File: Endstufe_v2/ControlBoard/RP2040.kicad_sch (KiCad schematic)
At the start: 33 parts, among them J5 DNP, J7 DNP, SW1 TS-1187A-B-A-B, SW2 TS-1187A-B-A-B, U2 TYPE-C 16PFS 2JCB1.2-H6.5 IPX8, U3 W25Q128JVS, U4 RP2040, Y1 12Mhz

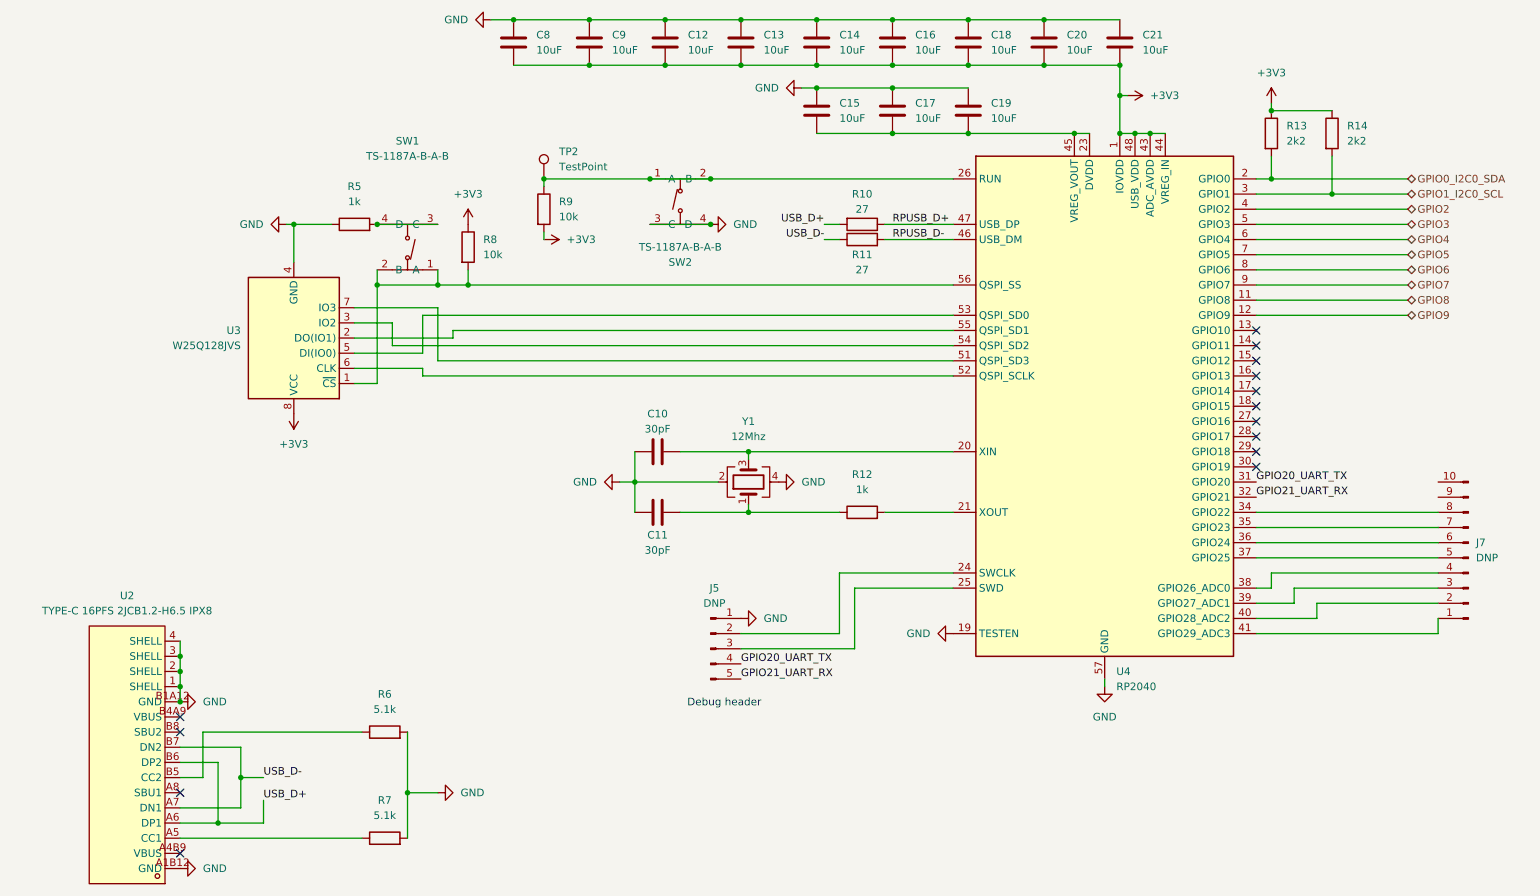
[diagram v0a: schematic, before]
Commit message: Added ADAU1962A DAC schematic
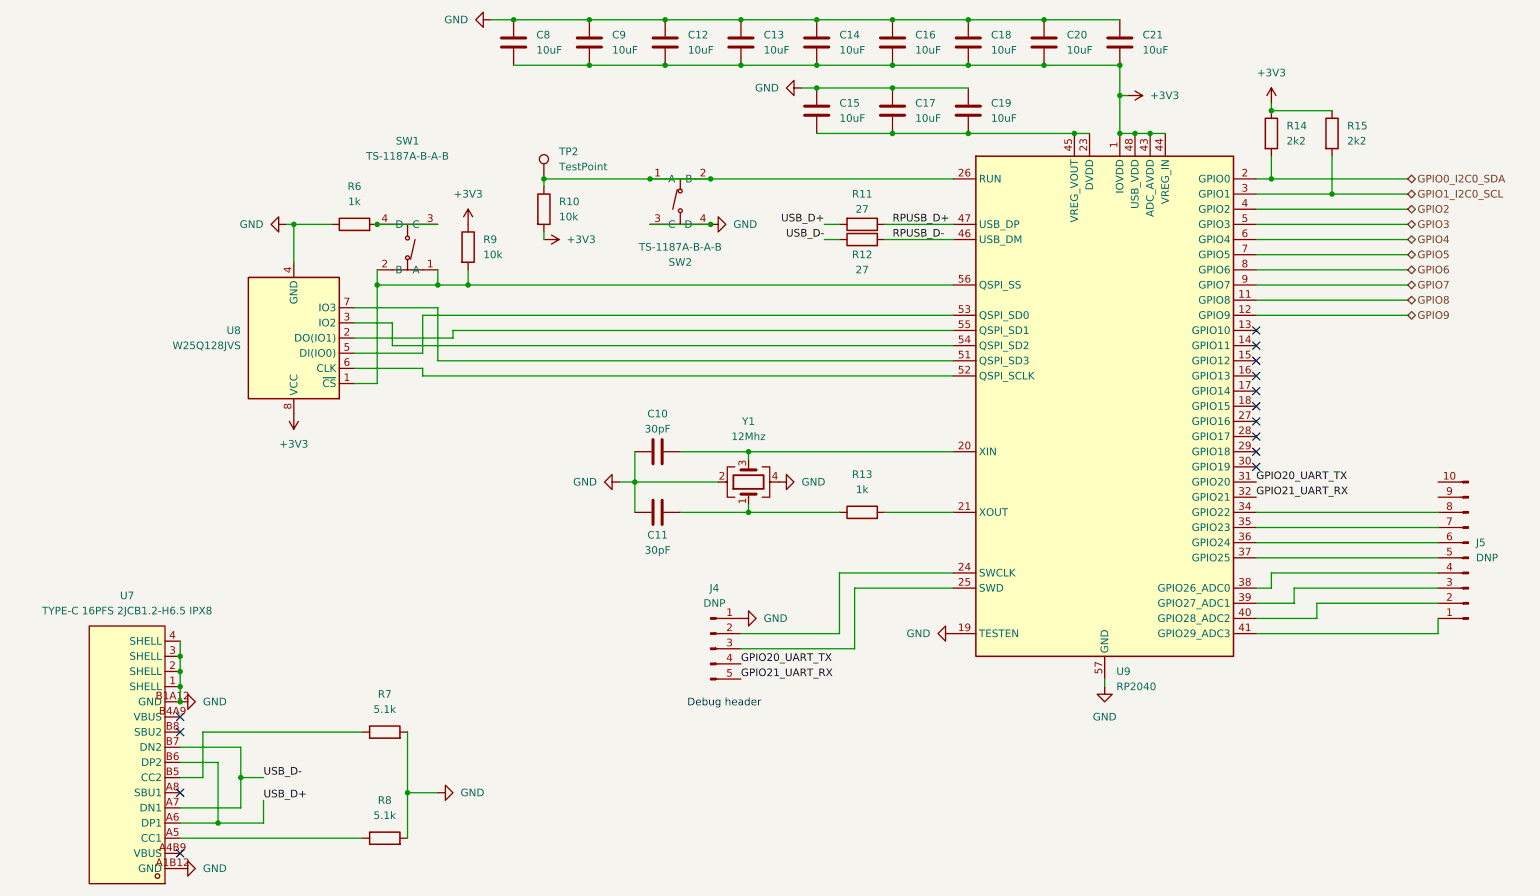
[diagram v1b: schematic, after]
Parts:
- renumbered J5 to J4, J7 to J5, R9 to R10, R10 to R11, R11 to R12, R12 to R13, R13 to R14, R14 to R15, R5 to R6, R6 to R7, R7 to R8, R8 to R9, U2 to U7, U3 to U8, U4 to U9

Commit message: Add footprints to all components
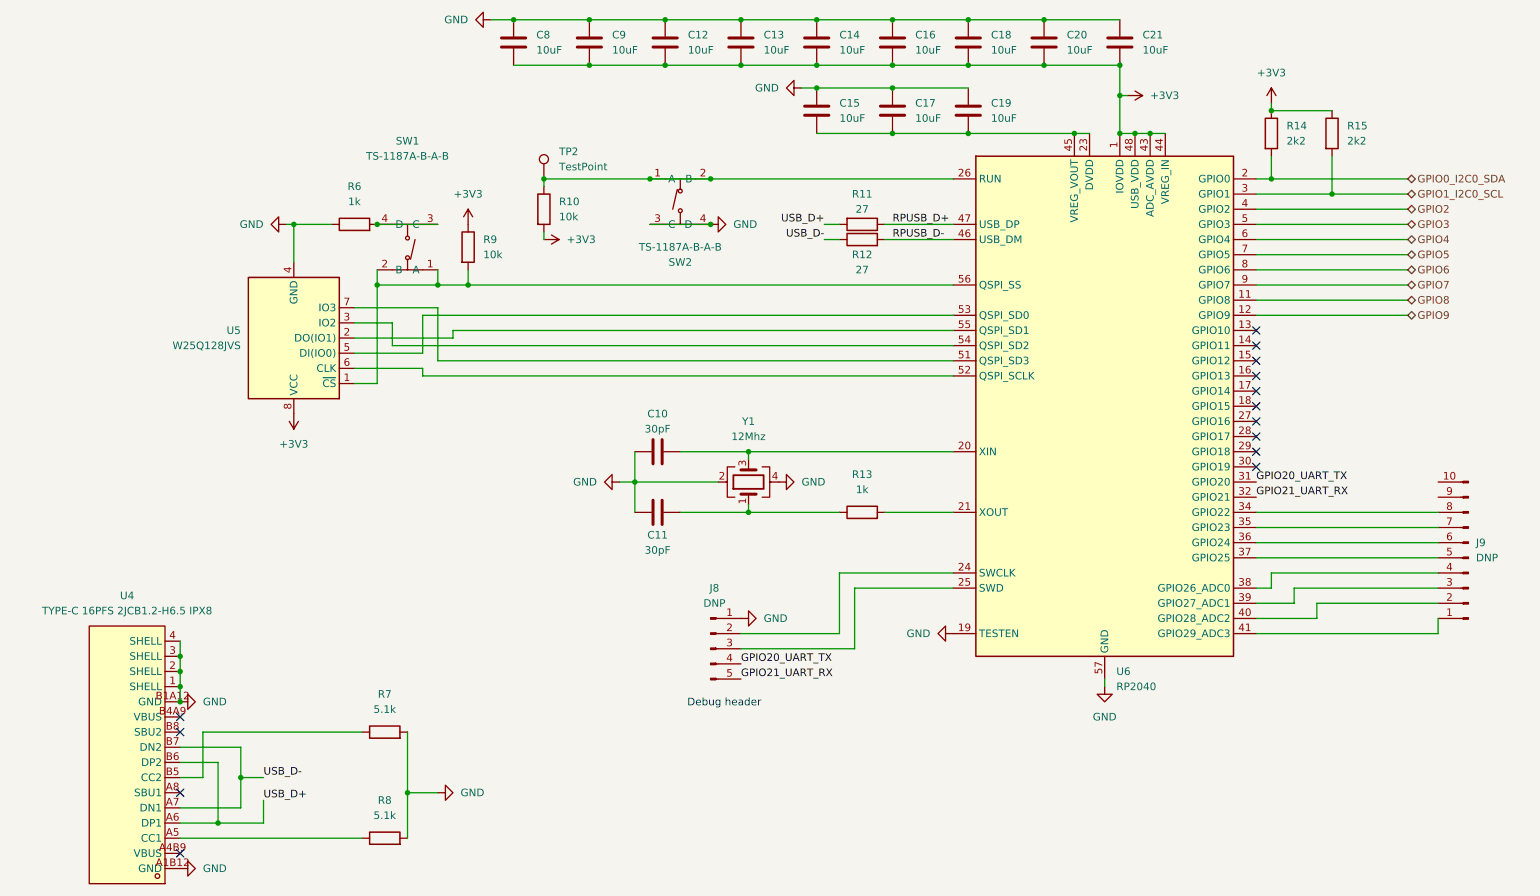
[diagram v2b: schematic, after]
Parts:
- J8: renamed from J4; footprint (none) -> Connector_PinHeader_2.54mm:PinHeader_1x05_P2.54mm_Vertical
- TP2: footprint (none) -> TestPoint:TestPoint_Pad_D1.0mm
- renumbered J5 to J9, U7 to U4, U8 to U5, U9 to U6
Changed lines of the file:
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@@
 		(dnp no)
 		(fields_autoplaced yes)
-		(property "Reference" "U7"
+		(property "Reference" "U4"
 			(at 36.83 123.19 0)
 			(effects
@@
 			(project "ControlBoard"
 				(path "/4f887f51-77c1-41d4-a3eb-45d362caffe1/2f61df4a-6dcc-4468-b102-34f7c082e72d"
-					(reference "U7")
+					(reference "U4")
 					(unit 1)
 				)
@@
 			)
 		)
-		(property "Footprint" ""
+		(property "Footprint" "TestPoint:TestPoint_Pad_D1.0mm"
 			(at 111.76 53.34 0)
 			(effects
@@
 		(dnp no)
 		(fields_autoplaced yes)
-		(property "Reference" "U9"
+		(property "Reference" "U6"
 			(at 202.6159 135.89 0)
 			(effects
@@
 			(project "ControlBoard"
 				(path "/4f887f51-77c1-41d4-a3eb-45d362caffe1/2f61df4a-6dcc-4468-b102-34f7c082e72d"
-					(reference "U9")
+					(reference "U6")
 					(unit 1)
 				)
@@
 		(on_board yes)
 		(dnp no)
-		(property "Reference" "J4"
+		(property "Reference" "J8"
 			(at 135.255 121.92 0)
 			(effects
@@
 			)
 		)
-		(property "Footprint" ""
+		(property "Footprint" "Connector_PinHeader_2.54mm:PinHeader_1x05_P2.54mm_Vertical"
 			(at 134.62 132.08 0)
 			(effects
@@
 			(project "ControlBoard"
 				(path "/4f887f51-77c1-41d4-a3eb-45d362caffe1/2f61df4a-6dcc-4468-b102-34f7c082e72d"
-					(reference "J4")
+					(reference "J8")
 					(unit 1)
 				)
@@
 		(dnp no)
 		(fields_autoplaced yes)
-		(property "Reference" "J5"
+		(property "Reference" "J9"
 			(at 262.89 114.3 0)
 			(effects
@@
 			(project "ControlBoard"
 				(path "/4f887f51-77c1-41d4-a3eb-45d362caffe1/2f61df4a-6dcc-4468-b102-34f7c082e72d"
-					(reference "J5")
+					(reference "J9")
 					(unit 1)
 				)
@@
 		(dnp no)
 		(fields_autoplaced yes)
-		(property "Reference" "U8"
+		(property "Reference" "U5"
 			(at 55.88 78.74 0)
 			(effects
@@
 			(project "ControlBoard"
 				(path "/4f887f51-77c1-41d4-a3eb-45d362caffe1/2f61df4a-6dcc-4468-b102-34f7c082e72d"
-					(reference "U8")
-					(unit 1)
-				)
+					(reference "U5")
+					(unit 1)
+				)

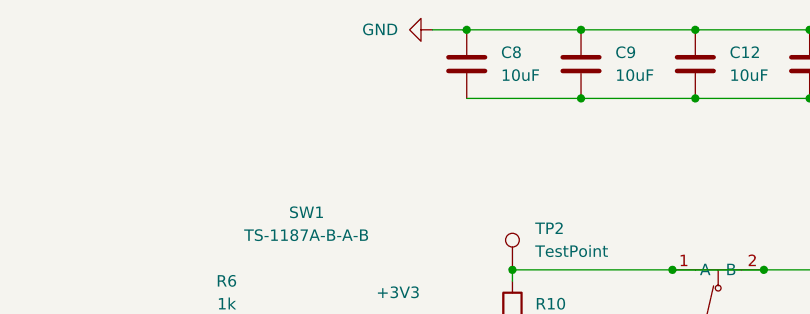
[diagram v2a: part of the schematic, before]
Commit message: Rough layout of components
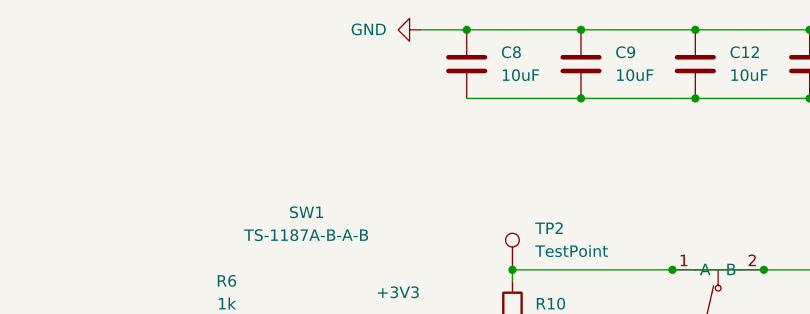
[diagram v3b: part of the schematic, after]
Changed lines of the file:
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@@
 	)
 	(junction
+		(at 114.3 34.29)
+		(diameter 0)
+		(color 0 0 0 0)
+	)
+	(junction
 		(at 152.4 38.1)
 		(diameter 0)
@@
 	)
 	(junction
-		(at 114.3 34.29)
-		(diameter 0)
-		(color 0 0 0 0)
-	)
-	(junction
 		(at 228.6 41.91)
 		(diameter 0)
@@
 	(wire
 		(pts
-			(xy 101.6 26.67) (xy 114.3 26.67)
+			(xy 96.52 26.67) (xy 101.6 26.67)
 		)
 		(stroke
@@
 	(wire
 		(pts
+			(xy 101.6 26.67) (xy 114.3 26.67)
+		)
+		(stroke
+			(width 0)
+			(type default)
+		)
+	)
+	(wire
+		(pts
 			(xy 83.82 156.21) (xy 88.9 156.21)
 		)
@@
 	(wire
 		(pts
+			(xy 101.6 34.29) (xy 114.3 34.29)
+		)
+		(stroke
+			(width 0)
+			(type default)
+		)
+	)
+	(wire
+		(pts
 			(xy 91.44 78.74) (xy 175.26 78.74)
 		)
@@
 	(wire
 		(pts
-			(xy 101.6 34.29) (xy 114.3 34.29)
-		)
-		(stroke
-			(width 0)
-			(type default)
-		)
-	)
-	(wire
-		(pts
 			(xy 78.74 68.58) (xy 78.74 71.12)
 		)
@@
 	(wire
 		(pts
-			(xy 97.79 26.67) (xy 101.6 26.67)
-		)
-		(stroke
-			(width 0)
-			(type default)
-		)
-	)
-	(wire
-		(pts
 			(xy 140.97 99.06) (xy 140.97 100.33)
 		)
@@
 	(symbol
 		(lib_id "Endstufe:C")
+		(at 101.6 30.48 0)
+		(unit 1)
+		(exclude_from_sim no)
+		(in_bom yes)
+		(on_board yes)
+		(dnp no)
+		(fields_autoplaced yes)
+		(property "Reference" "C8"
+			(at 105.41 29.21 0)
+			(effects
+				(font
+					(size 1.27 1.27)
+				)
+				(justify left)
+			)
+		)
+		(property "Value" "10uF"
+			(at 105.41 31.75 0)
+			(effects
+				(font
+					(size 1.27 1.27)
+				)
+				(justify left)
+			)
+		)
+		(property "Footprint" "Endstufe:C_0402_1005Metric"
+			(at 102.5652 34.29 0)
+			(effects
+				(font
+					(size 1.27 1.27)
+				)
+				(hide yes)
+			)
+		)
+		(property "Datasheet" "~"
+			(at 101.6 30.48 0)
+			(effects
+				(font
+					(size 1.27 1.27)
+				)
+				(hide yes)
+			)
+		)
+		(property "Description" ""
+			(at 101.6 30.48 0)
+			(effects
+				(font
+					(size 1.27 1.27)
+				)
+				(hide yes)
+			)
+		)
+		(property "LCSC Part #" "C15525"
+			(at 101.6 30.48 0)
+			(effects
+				(font
+					(size 1.27 1.27)
+				)
+				(hide yes)
+			)
+		)
+		(pin "1"
+		)
+		(pin "2"
+		)
+		(instances
+			(project "ControlBoard"
+				(path "/4f887f51-77c1-41d4-a3eb-45d362caffe1/2f61df4a-6dcc-4468-b102-34f7c082e72d"
+					(reference "C8")
+					(unit 1)
+				)
+			)
+		)
+	)
+	(symbol
+		(lib_id "Endstufe:C")
 		(at 165.1 41.91 0)
 		(unit 1)
@@
 	(symbol
 		(lib_id "Endstufe:GND")
-		(at 97.79 26.67 270)
+		(at 96.52 26.67 270)
 		(unit 1)
 		(exclude_from_sim no)
@@
 		(fields_autoplaced yes)
 		(property "Reference" "#PWR025"
-			(at 91.44 26.67 0)
+			(at 90.17 26.67 0)
 			(effects
 				(font
@@
 		)
 		(property "Value" "GND"
-			(at 93.98 26.67 90)
+			(at 92.71 26.67 90)
 			(effects
 				(font
@@
 		)
 		(property "Footprint" ""
-			(at 97.79 26.67 0)
+			(at 96.52 26.67 0)
 			(effects
 				(font
@@
 		)
 		(property "Datasheet" ""
-			(at 97.79 26.67 0)
+			(at 96.52 26.67 0)
 			(effects
 				(font
@@
 		)
 		(property "Description" ""
-			(at 97.79 26.67 0)
+			(at 96.52 26.67 0)
 			(effects
 				(font
@@
 					(unit 1)
 				)
-			)
-		)
-	)
-	(symbol
-		(lib_id "Endstufe:C")
-		(at 101.6 30.48 0)
-		(unit 1)
-		(exclude_from_sim no)
-		(in_bom yes)
-		(on_board yes)
-		(dnp no)
-		(fields_autoplaced yes)
-		(property "Reference" "C8"
-			(at 105.41 29.21 0)
-			(effects
-				(font
-					(size 1.27 1.27)
-				)
-				(justify left)
-			)
-		)
-		(property "Value" "10uF"
-			(at 105.41 31.75 0)
-			(effects
-				(font
-					(size 1.27 1.27)
-				)
-				(justify left)
-			)
-		)
-		(property "Footprint" "Endstufe:C_0402_1005Metric"
-			(at 102.5652 34.29 0)
-			(effects
-				(font
-					(size 1.27 1.27)
-				)
-				(hide yes)
-			)
-		)
-		(property "Datasheet" "~"
-			(at 101.6 30.48 0)
-			(effects
-				(font
-					(size 1.27 1.27)
-				)
-				(hide yes)
-			)
-		)
-		(property "Description" ""
-			(at 101.6 30.48 0)
-			(effects
-				(font
-					(size 1.27 1.27)
-				)
-				(hide yes)
-			)
-		)
-		(property "LCSC Part #" "C15525"
-			(at 101.6 30.48 0)
-			(effects
-				(font
-					(size 1.27 1.27)
-				)
-				(hide yes)
-			)
-		)
-		(pin "1"
-		)
-		(pin "2"
-		)
-		(instances
-			(project "ControlBoard"
-				(path "/4f887f51-77c1-41d4-a3eb-45d362caffe1/2f61df4a-6dcc-4468-b102-34f7c082e72d"
-					(reference "C8")
-					(unit 1)
-				)

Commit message: Continue layouting
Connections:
- net GPIO10: now reaches U6.13 (GPIO10)
- no-connect marks 14 -> 13
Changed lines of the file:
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@@
-	)
-	(no_connect
-		(at 226.06 78.74)
 	)
 	(no_connect
@@
 		(pts
 			(xy 226.06 60.96) (xy 251.46 60.96)
+		)
+		(stroke
+			(width 0)
+			(type default)
+		)
+	)
+	(wire
+		(pts
+			(xy 226.06 78.74) (xy 251.46 78.74)
 		)
 		(stroke
@@
 		(fields_autoplaced yes)
 		(effects
+			(font
+				(size 1.27 1.27)
+			)
+			(justify left)
+		)
+	)
+	(hierarchical_label "GPIO10"
+		(shape bidirectional)
+		(at 251.46 78.74 0)
+		(fields_autoplaced yes)
+		(effects

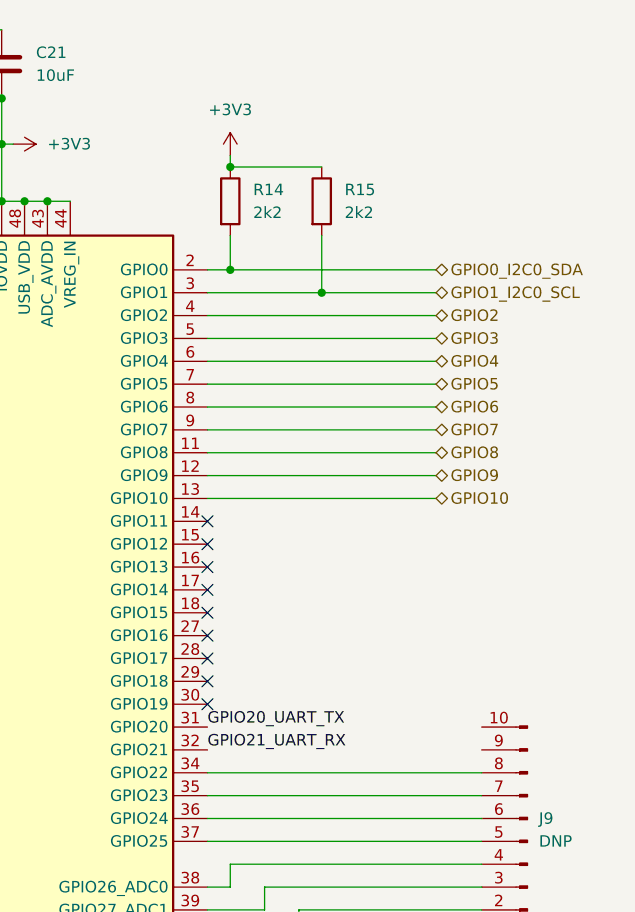
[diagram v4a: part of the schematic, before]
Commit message: Add additional I2C headers
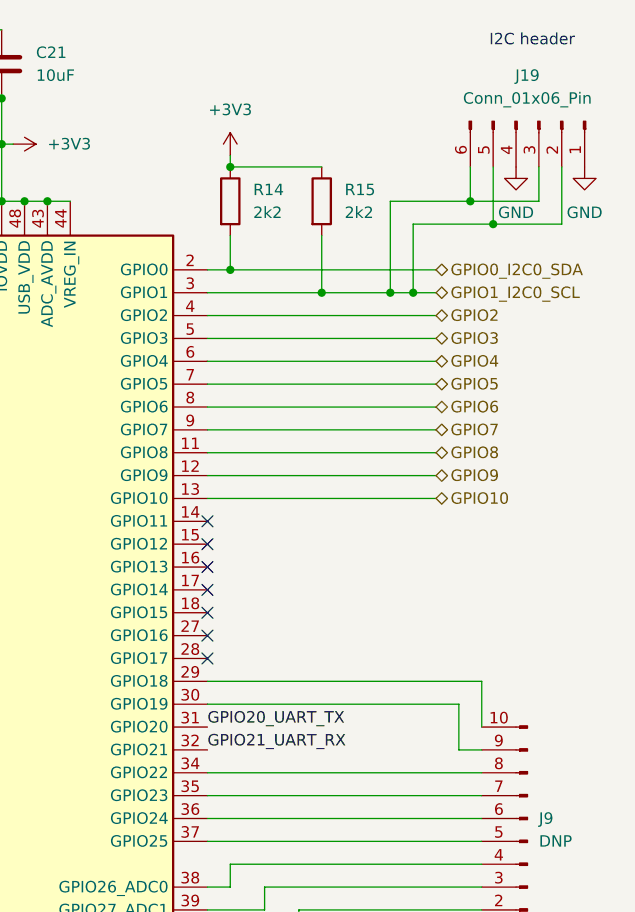
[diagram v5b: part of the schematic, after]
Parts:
- added J19: Conn_01x06_Pin, Connector_PinHeader_2.54mm:PinHeader_1x06_P2.54mm_Vertical, symbol Connector:Conn_01x06_Pin
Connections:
- net GND: now also J19.1 (Pin_1), J19.4 (Pin_4)
- net GPIO1_I2C0_SCL: now also J19.2 (Pin_2), J19.3 (Pin_3), J19.5 (Pin_5), J19.6 (Pin_6)
- net at U6.29 (GPIO18): now also J9.10 (Pin_10)
- net at U6.30 (GPIO19): now also J9.9 (Pin_9)
- no-connect marks 13 -> 11
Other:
- note added: "I2C header"

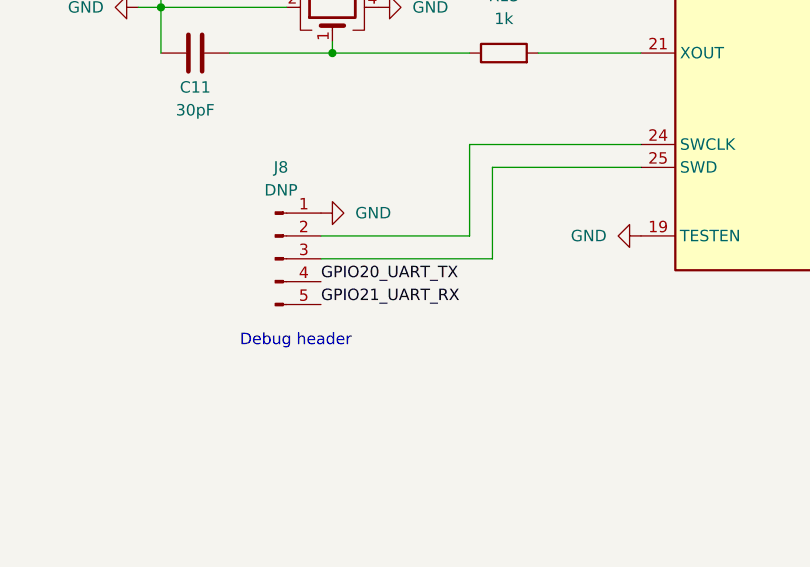
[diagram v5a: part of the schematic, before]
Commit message: Route control board (continued)
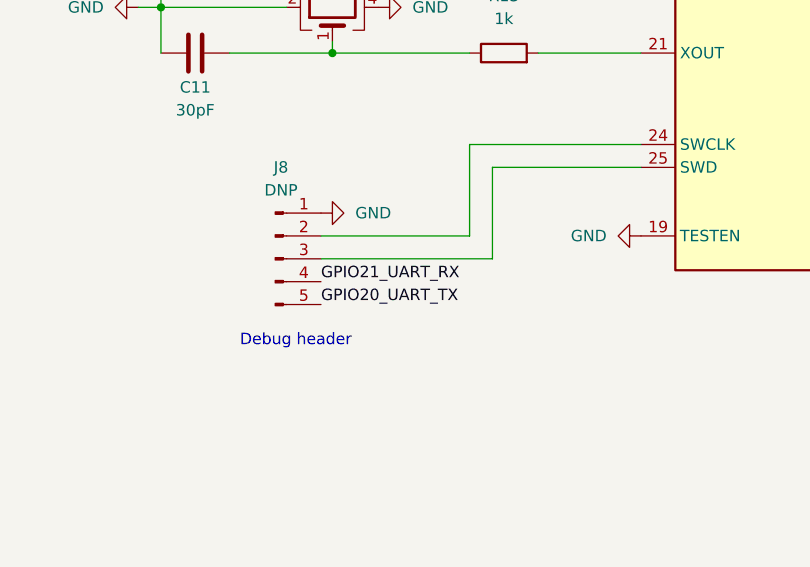
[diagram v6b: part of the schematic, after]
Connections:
- net GPIO20_UART_TX: now also J8.5 (Pin_5); no longer J8.4 (Pin_4)
- net GPIO21_UART_RX: now also J8.4 (Pin_4); no longer J8.5 (Pin_5)
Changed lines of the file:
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@@
-		)
-	)
-	(label "GPIO20_UART_TX"
-		(at 139.7 134.62 0)
-		(fields_autoplaced yes)
-		(effects
-			(font
-				(size 1.27 1.27)
-			)
-			(justify left bottom)
 		)
 	)
@@
 	)
 	(label "GPIO21_UART_RX"
-		(at 139.7 137.16 0)
+		(at 139.7 134.62 0)
 		(fields_autoplaced yes)
 		(effects
@@
 		(fields_autoplaced yes)
 		(effects
+			(font
+				(size 1.27 1.27)
+			)
+			(justify left bottom)
+		)
+	)
+	(label "GPIO20_UART_TX"
+		(at 139.7 137.16 0)
+		(fields_autoplaced yes)
+		(effects
